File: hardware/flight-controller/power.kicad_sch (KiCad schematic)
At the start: 0 parts

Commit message: sensors, power, actuators, filters
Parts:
- added C1, C11, C2, C7, C8: 100n, symbol Device:C
- added C10, C14, C15, C17, C18, C3, C4, C5, C6, C9: 4u7, symbol Device:C
- added C12: 10u/50V, symbol Device:C
- added C13: 22u/50V, symbol Device:C
- added C16: 150p, symbol Device:C
- added D1: SS34, symbol Device:D_Schottky
- added D2: LED, symbol Device:LED
- added J1, J3: XT-60, symbol Connector_Generic:Conn_01x02
- added J2, J4, J5, J6, J7: Conn_01x03, symbol Connector_Generic:Conn_01x03
- added L1, L2, L4, L5: 2u2, symbol Device:L
- added L3: 22u, symbol Device:L
- added Q1: IRFR5305, symbol Device:Q_PMOS_GDS
- added R1: 2m/1%, symbol Device:R
- added R10, R4: 1k, symbol Device:R
- added R11, R9: 100k, symbol Device:R
- added R2: 10k, symbol Device:R
- added R3, R6: 10, symbol Device:R
- added R5: 4k7, symbol Device:R
- added R7: 200k, symbol Device:R
- added R8: 39k, symbol Device:R
- added SW1: SW_Push_SPDT, symbol Switch:SW_Push_SPDT
- added U1: INA226, Package_SO:VSSOP-10_3x3mm_P0.5mm, symbol Sensor_Energy:INA226
- added U2: LM1117MP-3.3, Package_TO_SOT_SMD:SOT-223-3_TabPin2, symbol Regulator_Linear:LM1117MP-3.3
- added U3: MP1584, Package_SO:SOIC-8-1EP_3.9x4.9mm_P1.27mm_EP2.62x3.51mm_ThermalVias, symbol goose:MP1584
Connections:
- new net: C7.1, U3.8 (BST)
- new net: C16.2, R11.1
- new net: C2.1, R3.2, U1.10 (Vin+)
- new net: C2.2, R6.2, U1.8 (Vbus), U1.9 (Vin-)
- new net: R4.2, SW1.2 (B)
- new net: D2.2 (A), R10.2
- new net +3.3V: C1.1, C10.1, C11.1, R10.1, R5.1, U1.6 (VS), U2.2 (VO)
- new net +5V: C13.1, C14.1, C17.1, C3.1, C5.1, C8.1, C9.1, L1.1, L2.1, L3.2, L4.1, L5.1, R7.1, U2.3 (VI)
- new net BATTERY_IN: J3.2 (Pin_2), Q1.3 (S), R2.1
- new net COMP: C16.1, U3.3 (COMP)
- new net ESC: J2.1 (Pin_1)
- new net FB: R7.2, R8.1, U3.4 (FB)
- new net FREQ: R9.1, U3.6 (FREQ)
- new net GND: C1.2, C10.2, C11.2, C12.2, C13.2, C14.2, C15.2, C17.2, C18.2, C3.2, C4.2, C5.2, C6.2, C8.2, C9.2, D1.2 (A), D2.1 (K), J1.1 (Pin_1), J2.3 (Pin_3), J3.1 (Pin_1), J4.3 (Pin_3), J5.3 (Pin_3), J6.3 (Pin_3), J7.3 (Pin_3), R11.2, R8.2, R9.2, SW1.1 (A), U1.1 (A1), U1.2 (A0), U1.7 (GND), U2.1 (GND), U3.5 (GND)
- new net MOSFET_GATE: Q1.1 (G), R2.2, R4.1
- new net SENSOR_INT: R5.2, U1.3 (~{Alert})
- new net SENSOR_SCL: U1.5 (SCL)
- new net SENSOR_SDA: U1.4 (SDA)
- new net SERVO1: J4.1 (Pin_1)
- new net SERVO1_5V: C4.1, J4.2 (Pin_2), L1.2
- new net SERVO2: J5.1 (Pin_1)
- new net SERVO2_5V: C6.1, J5.2 (Pin_2), L2.2
- new net SERVO3: J6.1 (Pin_1)
- new net SERVO3_5V: C15.1, J6.2 (Pin_2), L4.2
- new net SERVO4: J7.1 (Pin_1)
- new net SERVO4_5V: C18.1, J7.2 (Pin_2), L5.2
- new net SUPPLY: Q1.2 (D), R1.1, R3.1
- new net SW: C7.2, D1.1 (K), L3.1, U3.1 (SW)
- new net VBUS: C12.1, J1.2 (Pin_2), R1.2, R6.1, U3.7 (VIN)
- no-connect marks 0 -> 3
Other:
- note added: "3.3V LDO regulator"
- note added: "5V STEP-DOWN converter"
- note added: "I2C address: 0x40 (7-bit)"
- note added: "actuators"
- note added: "power supply input"
- note added: "power supply measurement"
- note added: "should be 0.8V"

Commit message: schematic cleanup
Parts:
- removed C1, C2: 100n, symbol Device:C
- removed C14, C15, C17, C18, C3, C4, C5, C6: 4u7, symbol Device:C
- removed J1: XT-60, symbol Connector_Generic:Conn_01x02
- removed J2, J4, J5, J6, J7: Conn_01x03, symbol Connector_Generic:Conn_01x03
- removed L1, L2, L4, L5: 2u2, symbol Device:L
- removed R3, R6: 10, symbol Device:R
- removed R5: 4k7, symbol Device:R
- removed U1: INA226, Package_SO:VSSOP-10_3x3mm_P0.5mm, symbol Sensor_Energy:INA226
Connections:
- net SUPPLY renamed SHUNT_HIGH
- no-connect marks 3 -> 2
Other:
- note added: "3.3V domain"
- note added: "5V domain"
- note added: "power input"
- note removed: "3.3V LDO regulator"
- note removed: "5V STEP-DOWN converter"
- note removed: "I2C address: 0x40 (7-bit)"
- note removed: "actuators"
- note removed: "power supply input"
- note removed: "power supply measurement"
- moved on the sheet: C10, C11, C12, C13, C16, C7, C8, C9, D1, D2, J3, L3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

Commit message: still working
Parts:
- added C1, C2: 100n, Capacitor_SMD:C_0603_1608Metric, symbol Device:C
- added R3, R6: 10, Resistor_SMD:R_0603_1608Metric, symbol Device:R
- added R4: 4k7, Resistor_SMD:R_0603_1608Metric, symbol Device:R
- added U1: INA226, Package_SO:VSSOP-10_3x3mm_P0.5mm, symbol Sensor_Energy:INA226
- C10: renamed from C16; footprint (none) -> Capacitor_SMD:C_0603_1608Metric
- C3: renamed from C7; footprint (none) -> Capacitor_SMD:C_0603_1608Metric
- C4: renamed from C8; footprint (none) -> Capacitor_SMD:C_0603_1608Metric
- C5: renamed from C9; footprint (none) -> Capacitor_SMD:C_0603_1608Metric
- C7: renamed from C11; footprint (none) -> Capacitor_SMD:C_0603_1608Metric
- D2: value LED -> RED; footprint (none) -> Capacitor_SMD:C_0603_1608Metric
- J1: renamed from J3; footprint (none) -> Connector_AMASS:AMASS_XT60PW-M_1x02_P7.20mm_Horizontal
- Q1: footprint (none) -> Package_TO_SOT_SMD:TO-252-2
- R10, R11, R2, R7, R8, R9: footprint (none) -> Resistor_SMD:R_0603_1608Metric
- R5: renamed from R4; footprint (none) -> Resistor_SMD:R_0603_1608Metric
- renumbered C10 to C6, C12 to C8, C13 to C9, L3 to L1
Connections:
- net +3.3V: now also C1.1, R4.1, U1.6 (VS)
- net GND: now also C1.2, U1.1 (A1), U1.2 (A0), U1.7 (GND)
- net SHUNT_HIGH: now also R3.1
- net VBUS: now also R6.1
- new net: C2.1, R3.2, U1.10 (Vin+)
- new net: C2.2, R6.2, U1.8 (Vbus), U1.9 (Vin-)
- new net MISC_SCL: U1.5 (SCL)
- new net MISC_SDA: U1.4 (SDA)
- new net PWR_INT: R4.2, U1.3 (~{Alert})
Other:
- note added: "I2C address: 0x40 (7-bit)"
- note added: "power monitor"
- moved on the sheet: C10, C3, C4, C5, C6, C7, C8, C9, D1, D2, L1, R1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

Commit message: clean footprints
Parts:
- D1: footprint (none) -> Diode_SMD:D_MELF
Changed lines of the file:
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@@
 			)
 		)
-		(property "Footprint" ""
+		(property "Footprint" "Diode_SMD:D_MELF"
 			(at 74.93 119.38 0)
 			(effects

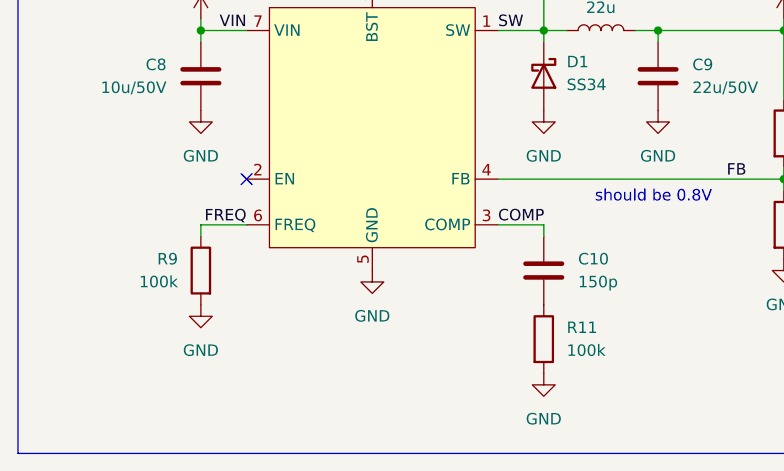
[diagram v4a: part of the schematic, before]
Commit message: more clean footprints
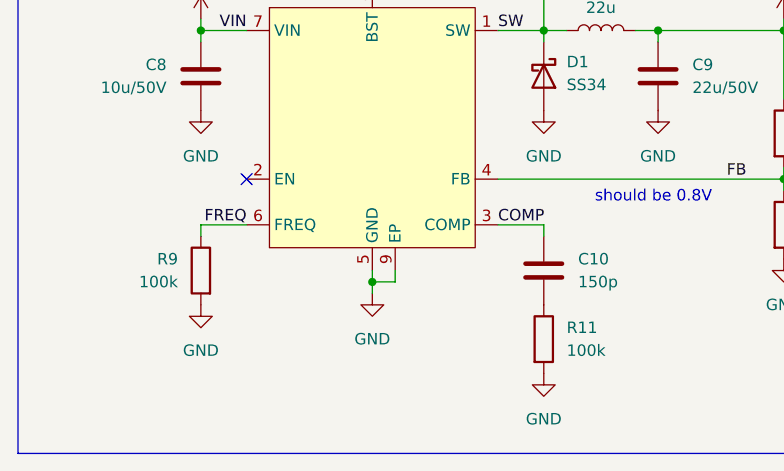
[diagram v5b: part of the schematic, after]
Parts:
- U3: footprint Package_SO:SOIC-8-1EP_3.9x4.9mm_P1.27mm_EP2.62x3.51mm_ThermalVias -> goose:mp1584
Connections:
- net GND: now also U3.9 (EP)
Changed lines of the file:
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@@
+	)
+	(junction
+		(at 55.88 142.24)
+		(diameter 0)
+		(color 0 0 0 0)
 	)
 	(junction
@@
 	(wire
 		(pts
+			(xy 55.88 142.24) (xy 55.88 140.97)
+		)
+		(stroke
+			(width 0)
+			(type default)
+		)
+	)
+	(wire
+		(pts
 			(xy 36.83 114.3) (xy 41.91 114.3)
 		)
@@
 	(wire
 		(pts
+			(xy 55.88 143.51) (xy 55.88 142.24)
+		)
+		(stroke
+			(width 0)
+			(type default)
+		)
+	)
+	(wire
+		(pts
 			(xy 69.85 135.89) (xy 74.93 135.89)
 		)
@@
 	(wire
 		(pts
+			(xy 55.88 142.24) (xy 58.42 142.24)
+		)
+		(stroke
+			(width 0)
+			(type default)
+		)
+	)
+	(wire
+		(pts
 			(xy 74.93 106.68) (xy 74.93 114.3)
 		)
@@
 		(pts
 			(xy 157.48 52.07) (xy 160.02 52.07)
+		)
+		(stroke
+			(width 0)
+			(type default)
+		)
+	)
+	(wire
+		(pts
+			(xy 58.42 142.24) (xy 58.42 140.97)
 		)
 		(stroke
@@
 	(symbol
 		(lib_id "power:GND")
-		(at 55.88 140.97 0)
+		(at 55.88 143.51 0)
 		(unit 1)
 		(exclude_from_sim no)
@@
 		(fields_autoplaced yes)
 		(property "Reference" "#PWR018"
-			(at 55.88 147.32 0)
+			(at 55.88 149.86 0)
 			(effects
 				(font
@@
 		)
 		(property "Value" "GND"
-			(at 55.88 146.05 0)
+			(at 55.88 148.59 0)
 			(effects
 				(font
@@
 		)
 		(property "Footprint" ""
-			(at 55.88 140.97 0)
+			(at 55.88 143.51 0)
 			(effects
 				(font
@@
 		)
 		(property "Datasheet" ""
-			(at 55.88 140.97 0)
+			(at 55.88 143.51 0)
 			(effects
 				(font
@@
 		)
 		(property "Description" "Power symbol creates a global label with name \"GND\" , ground"
-			(at 55.88 140.97 0)
+			(at 55.88 143.51 0)
 			(effects
 				(font
@@
 			)
 		)
-		(property "Footprint" "Package_SO:SOIC-8-1EP_3.9x4.9mm_P1.27mm_EP2.62x3.51mm_ThermalVias"
+		(property "Footprint" "goose:mp1584"
 			(at 55.372 71.374 0)
 			(effects
@@
 		(pin "7"
 		)
+		(pin "9"
+		)
 		(instances

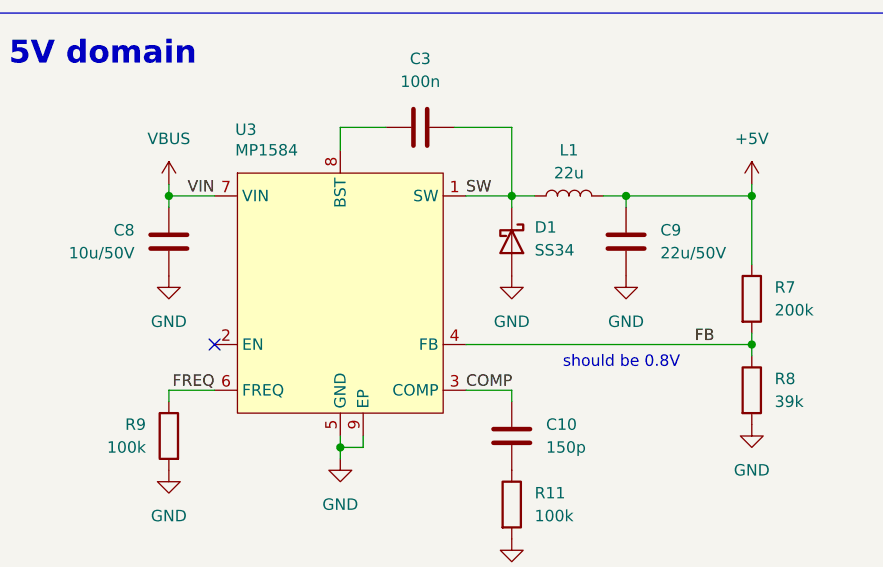
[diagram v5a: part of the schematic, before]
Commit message: clean footprints
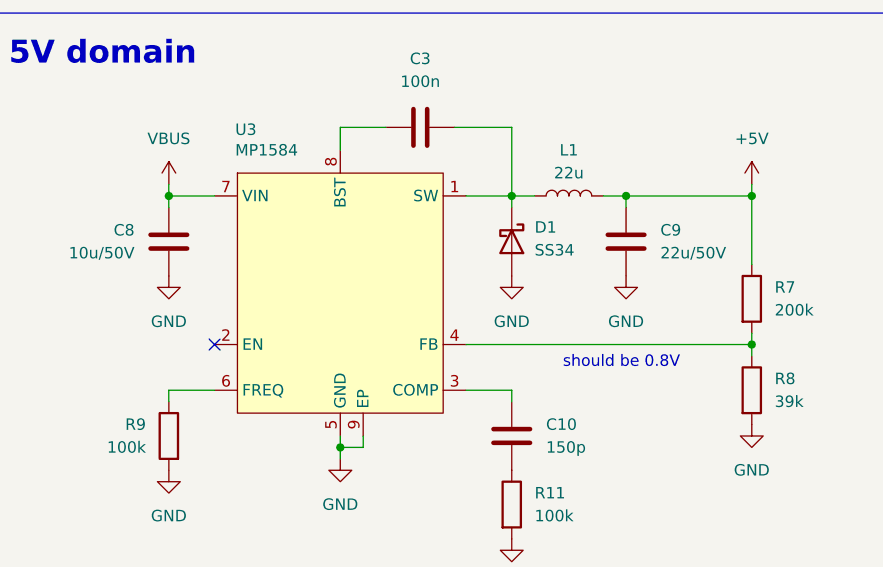
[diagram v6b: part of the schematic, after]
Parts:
- C6: footprint (none) -> Capacitor_SMD:C_0603_1608Metric
- D1: footprint Diode_SMD:D_MELF -> (none)
- D2: footprint Capacitor_SMD:C_0603_1608Metric -> LED_SMD:LED_0603_1608Metric
- J1: footprint Connector_AMASS:AMASS_XT60PW-M_1x02_P7.20mm_Horizontal -> goose:XT60PW-M
- Q1: footprint Package_TO_SOT_SMD:TO-252-2 -> goose:TO-252-2
- R1: footprint (none) -> Resistor_SMD:R_1206_3216Metric
- U1: footprint Package_SO:VSSOP-10_3x3mm_P0.5mm -> goose:INA226
- U2: footprint Package_TO_SOT_SMD:SOT-223-3_TabPin2 -> goose:LM1117-3.3
- U3: footprint goose:mp1584 -> goose:MP1584
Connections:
- net COMP: no longer names the net of C10.1, U3.3 (COMP)
- net FB: no longer names the net of R7.2, R8.1, U3.4 (FB)
- net FREQ: no longer names the net of R9.1, U3.6 (FREQ)
- net SW: no longer names the net of C3.2, D1.1 (K), L1.1, U3.1 (SW)
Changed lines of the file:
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@@
 		)
 	)
-	(label "COMP"
-		(at 69.85 135.89 0)
-		(fields_autoplaced yes)
-		(effects
-			(font
-				(size 1.27 1.27)
-			)
-			(justify left bottom)
-		)
-	)
-	(label "VIN"
-		(at 41.91 114.3 180)
-		(fields_autoplaced yes)
-		(effects
-			(font
-				(size 1.27 1.27)
-			)
-			(justify right bottom)
-		)
-	)
 	(label "SHUNT_HIGH"
 		(at 111.76 52.07 180)
@@
 		)
 	)
-	(label "FB"
-		(at 95.25 130.81 0)
-		(fields_autoplaced yes)
-		(effects
-			(font
-				(size 1.27 1.27)
-			)
-			(justify left bottom)
-		)
-	)
-	(label "SW"
-		(at 69.85 114.3 0)
-		(fields_autoplaced yes)
-		(effects
-			(font
-				(size 1.27 1.27)
-			)
-			(justify left bottom)
-		)
-	)
-	(label "FREQ"
-		(at 41.91 135.89 180)
-		(fields_autoplaced yes)
-		(effects
-			(font
-				(size 1.27 1.27)
-			)
-			(justify right bottom)
-		)
-	)
 	(global_label "PWR_INT"
 		(shape input)
@@
 			)
 		)
-		(property "Footprint" "Package_TO_SOT_SMD:TO-252-2"
+		(property "Footprint" "goose:TO-252-2"
 			(at 52.07 44.45 0)
 			(effects
@@
 			)
 		)
-		(property "Footprint" "goose:mp1584"
+		(property "Footprint" "goose:MP1584"
 			(at 55.372 71.374 0)
 			(effects
@@
 			)
 		)
-		(property "Footprint" "Package_TO_SOT_SMD:SOT-223-3_TabPin2"
+		(property "Footprint" "goose:LM1117-3.3"
 			(at 165.1 113.03 0)
 			(effects
@@
 			)
 		)
-		(property "Footprint" "Connector_AMASS:AMASS_XT60PW-M_1x02_P7.20mm_Horizontal"
+		(property "Footprint" "goose:XT60PW-M"
 			(at 21.59 49.53 0)
 			(effects
@@
 			)
 		)
-		(property "Footprint" ""
+		(property "Footprint" "Resistor_SMD:R_1206_3216Metric"
 			(at 71.12 48.768 90)
 			(effects
@@
 			)
 		)
-		(property "Footprint" "Diode_SMD:D_MELF"
+		(property "Footprint" ""
 			(at 74.93 119.38 0)
 			(effects
@@
 			)
 		)
-		(property "Footprint" "Capacitor_SMD:C_0603_1608Metric"
+		(property "Footprint" "LED_SMD:LED_0603_1608Metric"
 			(at 171.45 146.05 0)
 			(effects
@@
 			)
 		)
-		(property "Footprint" "Package_SO:VSSOP-10_3x3mm_P0.5mm"
+		(property "Footprint" "goose:INA226"
 			(at 167.64 68.58 0)
 			(effects
@@
 			)
 		)
-		(property "Footprint" ""
+		(property "Footprint" "Capacitor_SMD:C_0603_1608Metric"
 			(at 181.3052 121.92 0)
 			(effects

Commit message: clean models
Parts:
- removed R11: 100k, Resistor_SMD:R_0603_1608Metric, symbol Device:R
- removed U3: MP1584, goose:MP1584, symbol goose:MP1584
- added C11: 22n, Capacitor_SMD:C_0603_1608Metric, symbol Device:C
- added U3: VL14340, goose:LV14340, symbol goose:LV14340
- C10: value 150p -> 47u/16V; footprint Capacitor_SMD:C_0603_1608Metric -> Capacitor_SMD:C_1206_3216Metric
- C3: value 100n -> 100n/16V
- C5, C6: value 4u7 -> 4.7u
- C8: footprint (none) -> Capacitor_SMD:C_1206_3216Metric
- C9: value 22u/50V -> 47u/16V; footprint (none) -> Capacitor_SMD:C_1206_3216Metric
- D1: value SS34 -> ~; footprint (none) -> Diode_SMD:D_SMB
- L1: value 22u -> 6.8u/4.5A; footprint (none) -> goose:PA4341.XXXNLT
- R4: value 4k7 -> 4.7k
- R7: value 200k -> 100k
- R8: value 39k -> 49.9k
- R9: value 100k -> 17.8k
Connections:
- net +5V: now also C10.1
- net GND: now also C10.2, C11.2, U3.7 (GND), U3.9 (PAD)
- net VBUS: now also U3.2 (VIN)
- net at C3.2, D1.1 (K), L1.1: now also U3.8 (SW)
- net at R8.1: now also U3.4 (RT/SYNC); no longer R7.2
- net at R9.1: now also R7.2, U3.5 (FB)
- net at C3.1: now also U3.1 (BOOT)
- net MOSFET_GATE: no longer names the net of Q1.1 (G), R2.2, R5.1
- net SHUNT_HIGH: no longer names the net of Q1.2 (D), R1.1, R3.1
- new net: C11.1, U3.6 (SS)
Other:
- note added: "should be 0.75V"
- note removed: "should be 0.8V"
- moved on the sheet: R1

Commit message: switches footprints
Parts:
- SW1: footprint (none) -> goose:JS102011SAQN
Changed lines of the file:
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@@
 			)
 		)
-		(property "Footprint" ""
+		(property "Footprint" "goose:JS102011SAQN"
 			(at 49.53 71.12 0)
 			(effects
